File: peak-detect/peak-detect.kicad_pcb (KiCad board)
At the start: 4 copper layers, 33 x 59.7 mm, 70 parts, among them J1 Conn_02x05_Odd_Even, J2 CONN_01X03, J3 CONN_01X03, J4 CONN_01X03, J5 CONN_01X03, Q1 BC847, Q2 BC847, U1 OPA2134, U2 OPA2134, U3 OPA2134

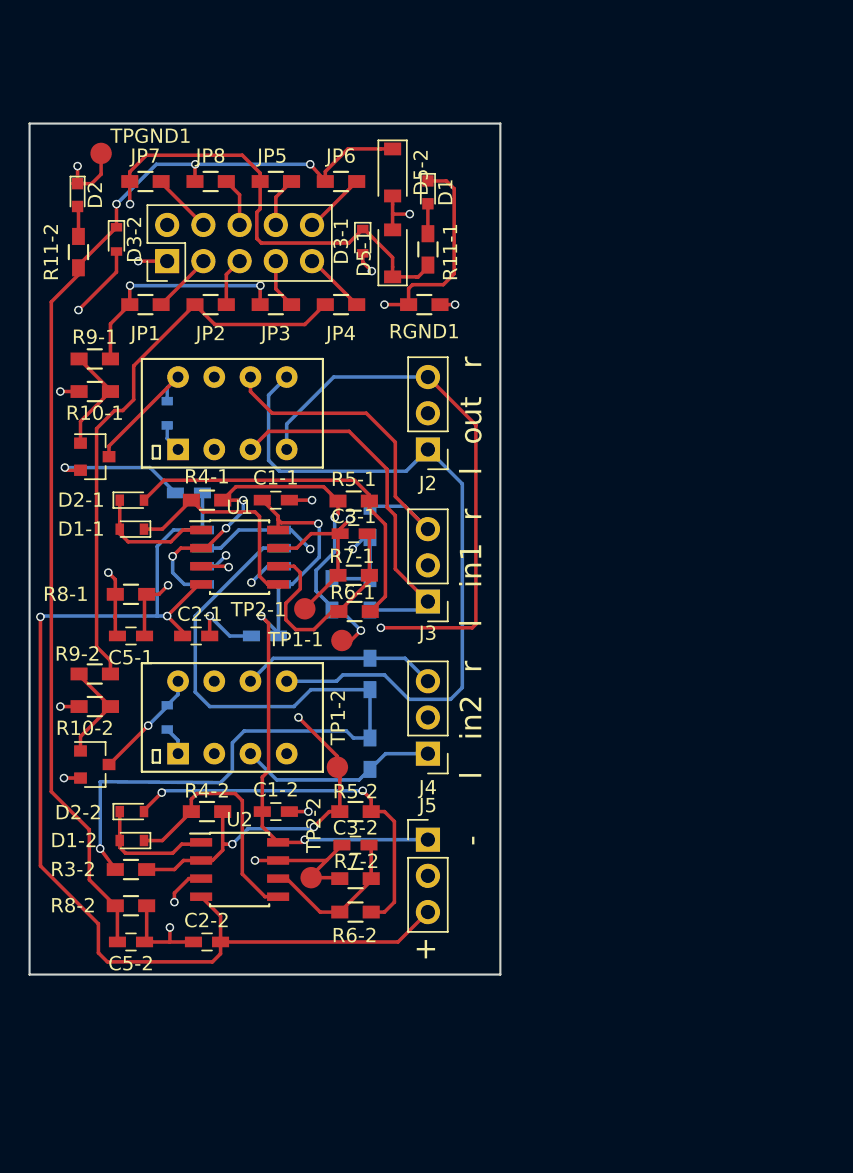
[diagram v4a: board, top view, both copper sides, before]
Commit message: peak-detect: add mixers humidity-sensor: fix bugs, smaller PCB
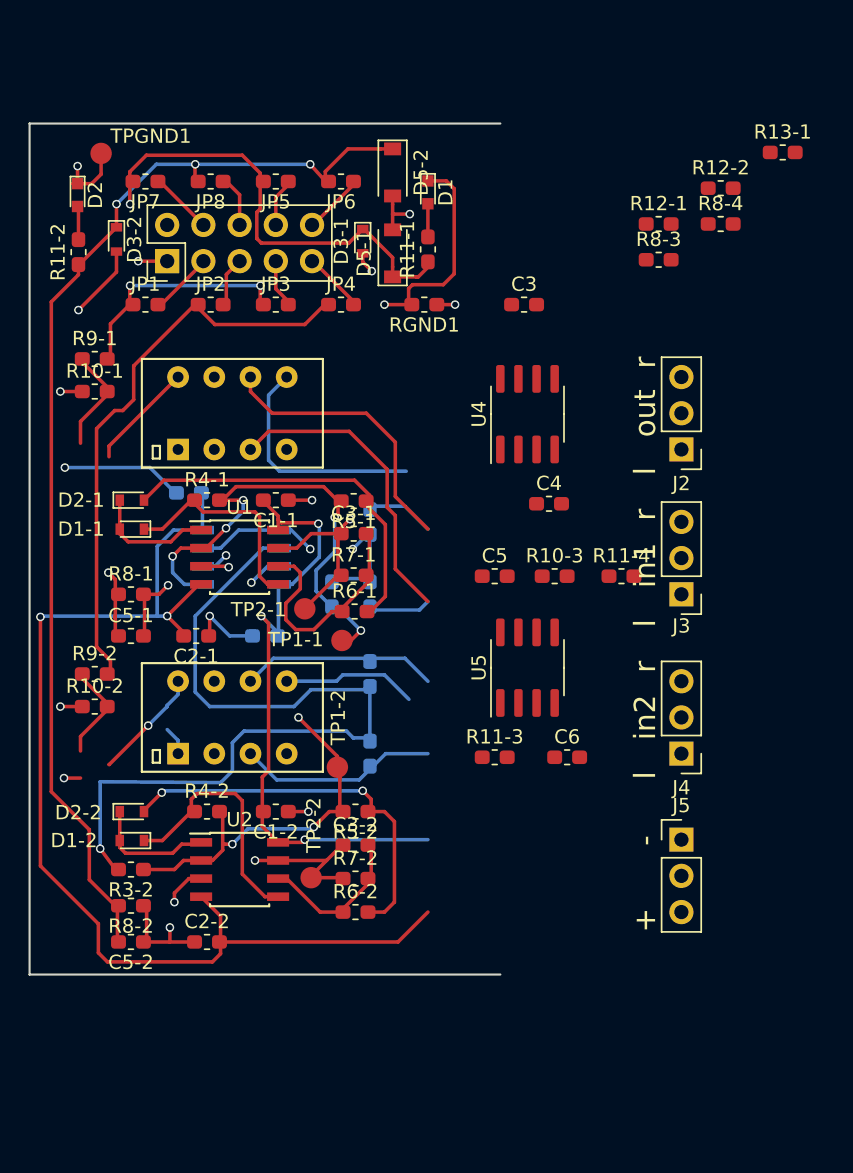
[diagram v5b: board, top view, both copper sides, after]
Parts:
- removed D4-1, D4-2: D, Diodes_SMD:D_0603
- removed Q1, Q2: BC847, TO_SOT_Packages_SMD:SOT-23
- added C3: 100nF, Capacitor_SMD:C_0603_1608Metric_Pad1.05x0.95mm_HandSolder, F.Cu at (192.2, 61.0)
- added C4: 100nF, Capacitor_SMD:C_0603_1608Metric_Pad1.05x0.95mm_HandSolder, F.Cu at (193.9, 74.9)
- added C5: 100nF, Capacitor_SMD:C_0603_1608Metric_Pad1.05x0.95mm_HandSolder, F.Cu at (190.1, 80.0)
- added C6: 100nF, Capacitor_SMD:C_0603_1608Metric_Pad1.05x0.95mm_HandSolder, F.Cu at (195.2, 92.7)
- added R10-3: 10k, Resistor_SMD:R_0603_1608Metric_Pad1.05x0.95mm_HandSolder, F.Cu at (194.3, 80.0)
- added R11-3: 10k, Resistor_SMD:R_0603_1608Metric_Pad1.05x0.95mm_HandSolder, F.Cu at (190.1, 92.7)
- added R11-4: 10k, Resistor_SMD:R_0603_1608Metric_Pad1.05x0.95mm_HandSolder, F.Cu at (199.0, 80.0)
- added R12-1: 10k, Resistor_SMD:R_0603_1608Metric_Pad1.05x0.95mm_HandSolder, F.Cu at (201.6, 55.3)
- added R12-2: 10k, Resistor_SMD:R_0603_1608Metric_Pad1.05x0.95mm_HandSolder, F.Cu at (206.0, 52.8)
- added R13-1: 10k, Resistor_SMD:R_0603_1608Metric_Pad1.05x0.95mm_HandSolder, F.Cu at (210.3, 50.3)
- added R8-3: 10k, Resistor_SMD:R_0603_1608Metric_Pad1.05x0.95mm_HandSolder, F.Cu at (201.6, 57.8)
- added R8-4: 10k, Resistor_SMD:R_0603_1608Metric_Pad1.05x0.95mm_HandSolder, F.Cu at (206.0, 55.3)
- added U4: OPA2134, Package_SO:SOIC-8_3.9x4.9mm_P1.27mm, F.Cu at (192.4, 68.6)
- added U5: OPA2134, Package_SO:SOIC-8_3.9x4.9mm_P1.27mm, F.Cu at (192.4, 86.4)
- C1, C1-1, C1-2, C2, C2-1, C2-2, C3-1, C3-2, C5-1, C5-2: footprint Capacitors_SMD:C_0603_HandSoldering -> Capacitor_SMD:C_0603_1608Metric_Pad1.05x0.95mm_HandSolder
- JP1, JP2, JP3, JP4, JP5, JP6, JP7, JP8, R1-1, R1-2, R11-1, R11-2, R2-1, R2-2, R3-1, R3-2, R4-1, R4-2, R5-1, R5-2, R6-1, R6-2, R7-1, R7-2, R8-1, R8-2, RGND1: footprint Resistors_SMD:R_0603_HandSoldering -> Resistor_SMD:R_0603_1608Metric_Pad1.05x0.95mm_HandSolder
- R10-1, R10-2, R9-1, R9-2: value 1k -> 10k; footprint Resistors_SMD:R_0603_HandSoldering -> Resistor_SMD:R_0603_1608Metric_Pad1.05x0.95mm_HandSolder
- moved J3 17.8 mm to (203.2, 81.3)
- moved J2 17.8 mm to (203.2, 71.1)
- moved J4 17.8 mm to (203.2, 92.5)
- moved J5 17.8 mm to (203.2, 98.5)
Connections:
- R10-1 pad 1: GNDD -> Out-Right-1
- R10-1 pad 2: Net-(Q1-Pad1) -> Net-(R10-1-Pad2)
- R10-2 pad 1: GNDD -> Out-Left-1
- R10-2 pad 2: Net-(Q2-Pad1) -> Net-(R10-2-Pad2)
- R9-1 pad 1: Net-(Q1-Pad1) -> Net-(R10-2-Pad2)
- R9-1 pad 2: Relay-1 -> Out-Left-1
- R9-2 pad 1: Net-(Q2-Pad1) -> Net-(R10-1-Pad2)
- R9-2 pad 2: Relay-2 -> Out-Right-1
- RL1 pad 3: In-Left-1 -> In-Left-2
- RL1 pad 6: In-Right-1 -> In-Right-2
- RL1 pad 8: Net-(D4-1-Pad2) -> Relay-2
- RL2 pad 3: In-Left-2 -> In-Left-1
- RL2 pad 6: In-Right-2 -> In-Right-1
- RL2 pad 8: Net-(D4-2-Pad2) -> Relay-1
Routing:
- net Out-Left: track 52.2 -> 0.00 mm, vias 1 -> 0
- net Out-Right: track 49.7 -> 25.8 mm
- net In-Left-1: track 26.0 -> 4.31 mm
- net In-Left-2: track 14.0 -> 35.6 mm
- net In-Right-2: track 13.8 -> 33.5 mm
- net In-Right-1: track 24.4 -> 4.73 mm
- net Net-(D4-1-Pad2): track 9.60 -> 0.00 mm
- net Net-(D4-2-Pad2): track 7.86 -> 0.00 mm, vias 1 -> 0
- net Relay-1: track 16.2 -> 24.1 mm, vias 2 -> 3
- net Relay-2: track 39.8 -> 47.4 mm
- net GNDD: track 58.2 -> 54.4 mm, vias 13 -> 11
- net +5V: track 49.8 -> 47.8 mm
- net Out-Right-1: track 0.00 -> 1.31 mm, vias 0 -> 1
- net Out-Left-1: track 0.00 -> 1.31 mm, vias 0 -> 1

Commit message: Give peak-detect a mute option
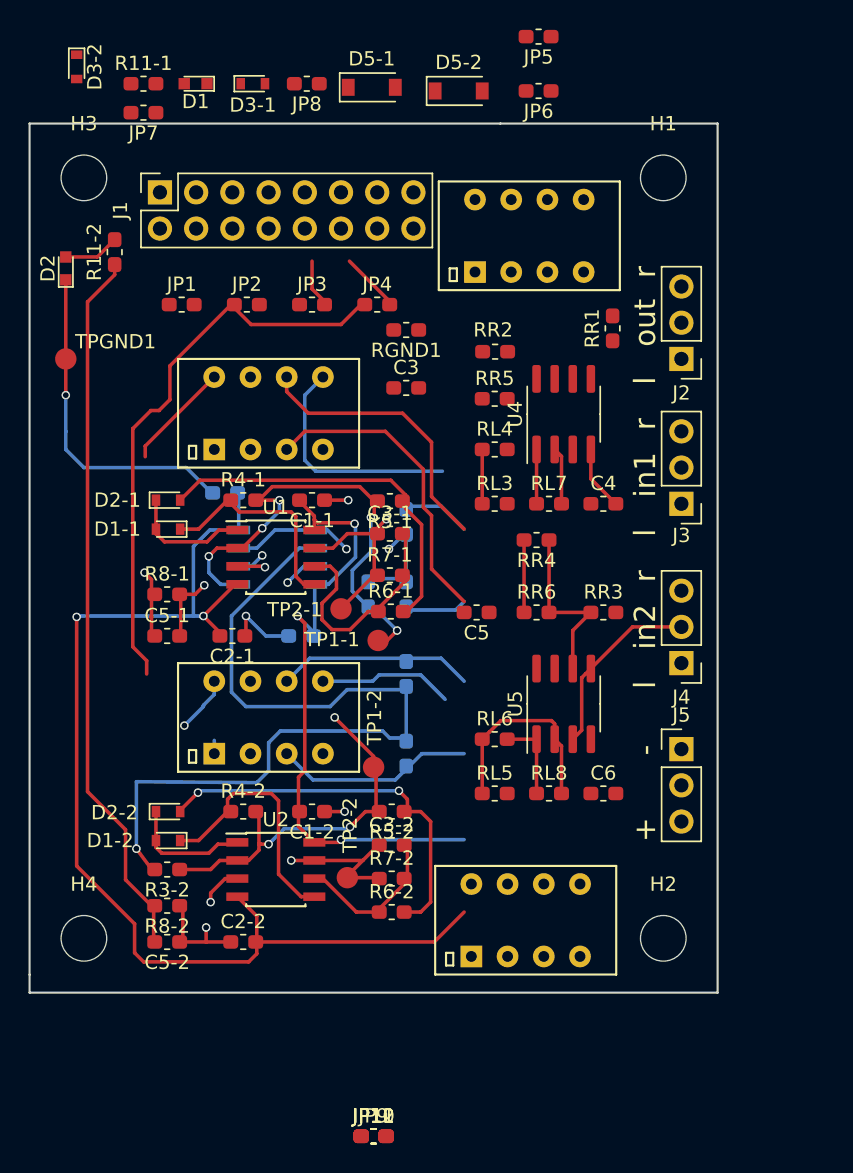
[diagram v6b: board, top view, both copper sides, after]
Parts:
- removed R10-1, R12-1: 10k, Resistor_SMD:R_0603_1608Metric_Pad1.05x0.95mm_HandSolder
- added H1: MountingHole, MountingHole:MountingHole_3.2mm_M3_DIN965, F.Cu at (201.9, 52.1)
- added H2: MountingHole, MountingHole:MountingHole_3.2mm_M3_DIN965, F.Cu at (201.9, 105.4)
- added H3: MountingHole, MountingHole:MountingHole_3.2mm_M3_DIN965, F.Cu at (161.3, 52.1)
- added H4: MountingHole, MountingHole:MountingHole_3.2mm_M3_DIN965, F.Cu at (161.3, 105.4)
- added JP10: Relay-6, Resistor_SMD:R_0603_1608Metric_Pad1.05x0.95mm_HandSolder, F.Cu at (181.6, 119.3)
- added JP11, JP12: Relay-7, Resistor_SMD:R_0603_1608Metric_Pad1.05x0.95mm_HandSolder, F.Cu at (181.6, 119.3)
- added JP9: Relay-5, Resistor_SMD:R_0603_1608Metric_Pad1.05x0.95mm_HandSolder, F.Cu at (181.6, 119.3)
- added RL10: Omron_G6K, lci-kicad:Omron-G6K, F.Cu at (192.3, 104.1)
- added RL6: 10k, Resistor_SMD:R_0603_1608Metric_Pad1.05x0.95mm_HandSolder, F.Cu at (190.1, 91.4)
- added RL9: Omron_G6K, lci-kicad:Omron-G6K, F.Cu at (192.5, 56.1)
- added RR5: 10k, Resistor_SMD:R_0603_1608Metric_Pad1.05x0.95mm_HandSolder, F.Cu at (190.1, 67.6)
- J1: value Conn_02x05_Odd_Even -> Conn_02x08_Odd_Even; footprint Pin_Headers:Pin_Header_Straight_2x05_Pitch2.54mm -> Connector_PinSocket_2.54mm:PinSocket_2x08_P2.54mm_Vertical
- moved RL8 47.9 mm to (193.9, 95.2)
- moved RR2 36.0 mm to (190.1, 64.3), turned to 180 degrees
- moved RL7 34.9 mm to (193.9, 74.9)
- moved RL4 28.8 mm to (190.1, 71.1)
- moved RR4 27.9 mm to (193.0, 77.5), turned to 180 degrees
- moved R11-1 23.1 mm to (165.5, 45.5), turned to 0 degrees
- moved JP5 21.0 mm to (193.2, 42.2)
- moved RL3 20.6 mm to (190.1, 74.9)
- moved D1 18.0 mm to (169.1, 45.5), turned to 180 degrees
- moved JP6 15.2 mm to (193.2, 46.0)
- moved TPGND1 14.6 mm to (160.0, 64.8)
- moved D3-1 13.5 mm to (173.1, 45.5), turned to 0 degrees
- moved D3-2 12.4 mm to (160.8, 44.3)
- moved D5-1 11.7 mm to (181.5, 45.7), turned to 0 degrees
- moved RR1 10.5 mm to (198.4, 62.6), turned to 90 degrees
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- renumbered R1-2 to RL1-1, R1-1 to RL1-2, R8-3 to RL3, R9-1 to RL4, R11-3 to RL5, R10-2 to RL7, R13-1 to RL8, R8-4 to RR1, R2-1 to RR1-1, R9-2 to RR2, R2-2 to RR2-1, R11-4 to RR3, R12-2 to RR4, R10-3 to RR6
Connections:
- net Out-Left-2 renamed Out-Left-Mixed-2
- RL1 pad 3: In-Left-2 -> Out-Left
- RL1 pad 4: Out-Left -> In-Left-2
- RL1 pad 5: Out-Right -> In-Right-2
- RL1 pad 6: In-Right-2 -> Out-Right
- RL2 pad 3: In-Left-1 -> Out-Left
- RL2 pad 4: Out-Left -> In-Left-1
- RL2 pad 5: Out-Right -> In-Right-1
- RL2 pad 6: In-Right-1 -> Out-Right
- RL7 pad 1: Out-Left-1 -> Out-Left-Mixed-1
- RR1 pad 1: Net-(R8-4-Pad1) -> Net-(RR1-Pad1)
- RR2 pad 1: Net-(R10-1-Pad2) -> Net-(RR1-Pad1)
- RR6 pad 1: Out-Right-2 -> Out-Right-Mixed-2
- U4 pad 1: Out-Left-1 -> Out-Left-Mixed-1
- U4 pad 6: Net-(R8-4-Pad1) -> Net-(RR1-Pad1)
- U4 pad 7: Out-Right-1 -> Out-Right-Mixed-1
- U5 pad 7: Out-Right-2 -> Out-Right-Mixed-2
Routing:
- net Out-Peak-1: track 68.2 -> 4.75 mm, vias 2 -> 1
- net Out-Peak-2: track 79.2 -> 50.2 mm, vias 3 -> 0
- net In-Left-2: track 35.6 -> 14.0 mm
- net Out-Left: track 0.00 -> 21.7 mm
- net Relay-1: track 24.1 -> 3.98 mm, vias 3 -> 1
- net +5V: track 47.8 -> 31.2 mm
- net Net-(RL5-Pad1): track 0.00 -> 14.6 mm
- net Net-(RR3-Pad1): track 0.00 -> 12.5 mm
- net GND: track 43.5 -> 55.5 mm, vias 4 -> 3
- net GNDD: track 54.4 -> 43.1 mm, vias 11 -> 6
- net In-Right-1: track 4.73 -> 14.2 mm
- net Net-(RL3-Pad1): track 0.00 -> 7.82 mm
- net Net-(Q1-Pad1): track 7.69 -> 0.00 mm
- net Net-(Q2-Pad1): track 7.18 -> 0.00 mm
- net Out-Right: track 25.8 -> 19.7 mm
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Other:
- board size 33 x 59.7 mm -> 48.3 x 61 mm

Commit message: WIP
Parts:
- moved JP9 67.9 mm to (179.3, 51.4), turned to 270 degrees
- moved JP10 67.9 mm to (181.9, 51.4), turned to 270 degrees
- moved JP11 58.3 mm to (181.9, 61.0), turned to 90 degrees
- moved JP12 58.1 mm to (179.6, 61.2), turned to 90 degrees
- moved D5-2 32.2 mm to (163.1, 66.9), turned to 270 degrees
- moved JP5 26.9 mm to (174.2, 61.3), turned to 270 degrees
- moved JP6 22.5 mm to (176.8, 61.3), turned to 270 degrees
- moved JP8 16.7 mm to (171.7, 61.3), turned to 270 degrees
- moved JP7 14.1 mm to (169.2, 61.1), turned to 270 degrees
- moved JP4 10.8 mm to (176.8, 51.4), turned to 270 degrees
- moved JP3 9.99 mm to (174.2, 51.4), turned to 270 degrees
- moved JP1 9.59 mm to (169.2, 51.4), turned to 270 degrees
- moved JP2 9.58 mm to (171.8, 51.4), turned to 270 degrees
- moved J1 2.03 mm to (166.6, 55.1)
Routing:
- net Relay-2: track 47.4 -> 7.59 mm
- net Net-(J1-Pad9): track 4.31 -> 0.00 mm
- net Net-(J1-Pad7): track 3.50 -> 0.00 mm

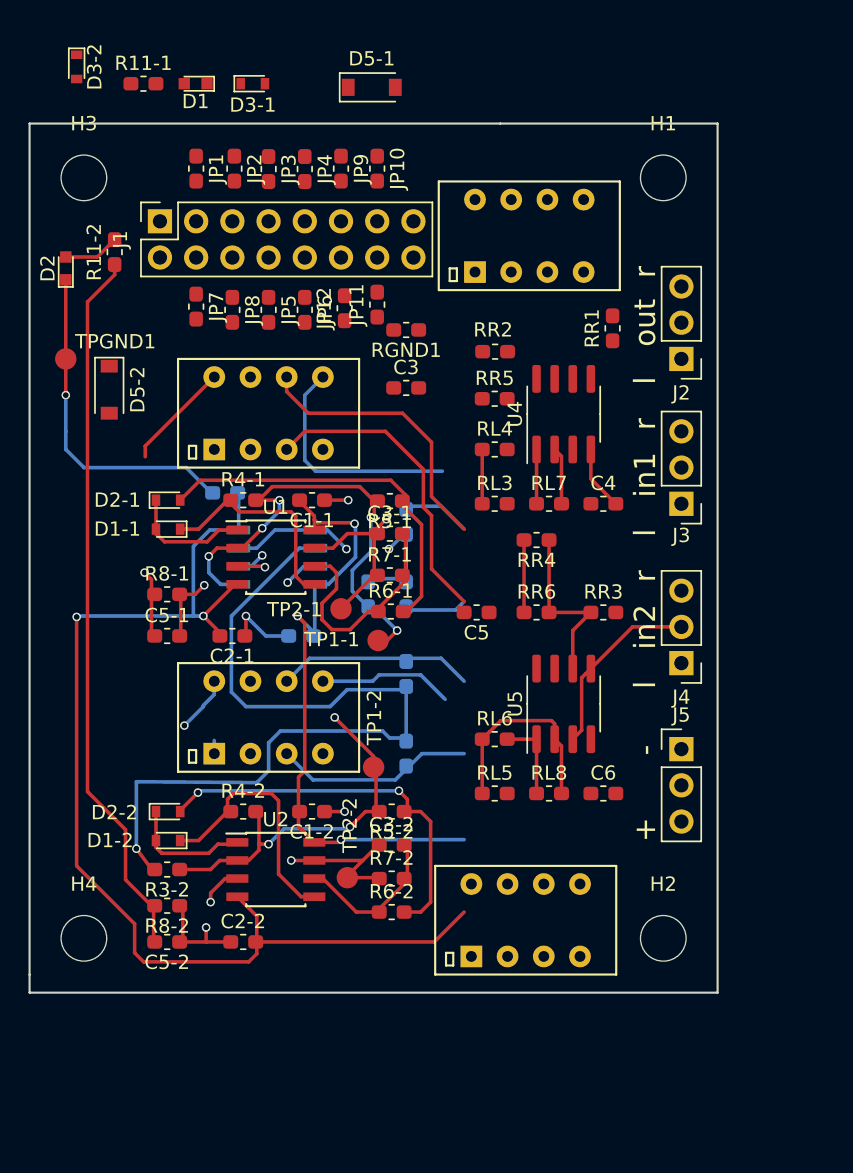
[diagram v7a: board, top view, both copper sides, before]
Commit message: Route mute, mostly automatic changes for peak-detect
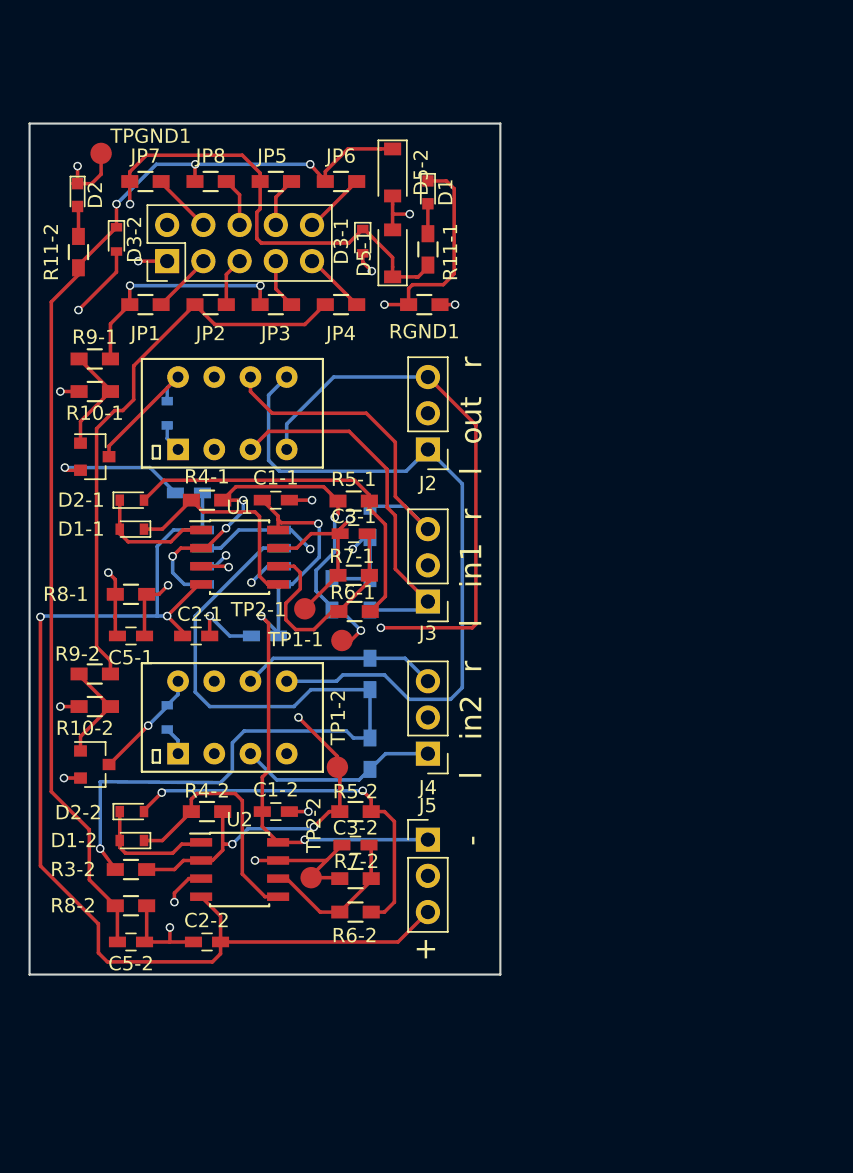
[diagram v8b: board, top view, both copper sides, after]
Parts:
- removed C3, C4, C5, C6: 100nF, Capacitor_SMD:C_0603_1608Metric_Pad1.05x0.95mm_HandSolder
- removed H1, H2, H3, H4: MountingHole, MountingHole:MountingHole_3.2mm_M3_DIN965
- removed JP10: Relay-6, Resistor_SMD:R_0603_1608Metric_Pad1.05x0.95mm_HandSolder
- removed JP11, JP12: Relay-7, Resistor_SMD:R_0603_1608Metric_Pad1.05x0.95mm_HandSolder
- removed JP9: Relay-5, Resistor_SMD:R_0603_1608Metric_Pad1.05x0.95mm_HandSolder
- removed RL1-1, RL1-2, RL3, RL4, RL5, RL6, RL7, RL8, RR1, RR1-1, RR2, RR2-1, RR3, RR4, RR5, RR6: 10k, Resistor_SMD:R_0603_1608Metric_Pad1.05x0.95mm_HandSolder
- removed RL10, RL9: Omron_G6K, lci-kicad:Omron-G6K
- removed U4, U5: OPA2134, Package_SO:SOIC-8_3.9x4.9mm_P1.27mm
- added D4-1: D, Diodes_SMD:D_0603, B.Cu at (167.1, 68.6)
- added D4-2: D, Diodes_SMD:D_0603, B.Cu at (167.1, 89.9)
- added Q1: BC847, TO_SOT_Packages_SMD:SOT-23, F.Cu at (162.1, 71.6)
- added Q2: BC847, TO_SOT_Packages_SMD:SOT-23, F.Cu at (162.1, 93.2)
- added R1-1: 10k, Resistors_SMD:R_0603_HandSoldering, B.Cu at (181.4, 81.3)
- added R1-2: 10k, Resistors_SMD:R_0603_HandSoldering, B.Cu at (181.4, 92.5)
- added R10-1: 1k, Resistors_SMD:R_0603_HandSoldering, F.Cu at (162.1, 67.1)
- added R10-2: 1k, Resistors_SMD:R_0603_HandSoldering, F.Cu at (162.1, 89.2)
- added R2-1: 10k, Resistors_SMD:R_0603_HandSoldering, B.Cu at (181.4, 76.2)
- added R2-2: 10k, Resistors_SMD:R_0603_HandSoldering, B.Cu at (181.4, 86.9)
- added R9-1: 1k, Resistors_SMD:R_0603_HandSoldering, F.Cu at (162.1, 64.8)
- added R9-2: 1k, Resistors_SMD:R_0603_HandSoldering, F.Cu at (162.1, 86.9)
- C1, C1-1, C1-2, C2, C2-1, C2-2, C3-1, C3-2, C5-1, C5-2: footprint Capacitor_SMD:C_0603_1608Metric_Pad1.05x0.95mm_HandSolder -> Capacitors_SMD:C_0603_HandSoldering
- J1: value Conn_02x08_Odd_Even -> Conn_02x05_Odd_Even; footprint Connector_PinSocket_2.54mm:PinSocket_2x08_P2.54mm_Vertical -> Pin_Headers:Pin_Header_Straight_2x05_Pitch2.54mm
- JP1, JP2, JP3, JP4, JP5, JP6, JP7, JP8, R11-1, R11-2, R3-1, R3-2, R4-1, R4-2, R5-1, R5-2, R6-1, R6-2, R7-1, R7-2, R8-1, R8-2, RGND1: footprint Resistor_SMD:R_0603_1608Metric_Pad1.05x0.95mm_HandSolder -> Resistors_SMD:R_0603_HandSoldering
- moved D5-2 25.0 mm to (182.9, 51.7)
- moved R11-1 23.1 mm to (185.4, 57.1), turned to 90 degrees
- moved J3 19.1 mm to (185.4, 81.8)
- moved J2 18.9 mm to (185.4, 71.1)
- moved J4 18.9 mm to (185.4, 92.5)
- moved J5 18.9 mm to (185.4, 98.5)
- moved D1 18.0 mm to (185.4, 53.1), turned to 270 degrees
- moved TPGND1 14.6 mm to (162.5, 50.4)
- moved D3-1 13.5 mm to (180.8, 56.5), turned to 270 degrees
- moved D3-2 12.4 mm to (163.6, 56.4)
- moved D5-1 11.7 mm to (182.9, 57.4), turned to 90 degrees
- moved JP1 10.2 mm to (165.6, 61.0), turned to 0 degrees
- moved JP4 9.84 mm to (179.3, 61.0), turned to 0 degrees
- moved JP2 9.68 mm to (170.2, 61.0), turned to 0 degrees
- moved JP3 9.52 mm to (174.8, 61.0), turned to 0 degrees
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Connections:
- RL1 pad 3: Out-Left -> In-Left-1
- RL1 pad 4: In-Left-2 -> Out-Left
- RL1 pad 5: In-Right-2 -> Out-Right
- RL1 pad 6: Out-Right -> In-Right-1
- RL1 pad 8: Relay-2 -> Net-(D4-1-Pad2)
- RL2 pad 3: Out-Left -> In-Left-2
- RL2 pad 4: In-Left-1 -> Out-Left
- RL2 pad 5: In-Right-1 -> Out-Right
- RL2 pad 6: Out-Right -> In-Right-2
- RL2 pad 8: Relay-1 -> Net-(D4-2-Pad2)
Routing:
- net Out-Peak-1: track 4.75 -> 68.2 mm, vias 1 -> 2
- net Relay-2: track 7.59 -> 39.8 mm
- net Out-Left: track 21.7 -> 52.2 mm, vias 0 -> 1
- net Out-Right: track 19.7 -> 49.7 mm
- net Out-Peak-2: track 50.2 -> 79.2 mm, vias 0 -> 3
- net In-Left-1: track 4.31 -> 26.0 mm
- net +5V: track 31.2 -> 49.8 mm
- net In-Right-2: track 30.1 -> 13.8 mm
- net GNDD: track 43.1 -> 58.2 mm, vias 6 -> 13
- net Net-(RL5-Pad1): track 14.6 -> 0.00 mm
- net Net-(RR3-Pad1): track 12.5 -> 0.00 mm
- net Relay-1: track 3.98 -> 16.2 mm, vias 1 -> 2
- net GND: track 55.5 -> 43.5 mm, vias 3 -> 4
- net In-Right-1: track 14.2 -> 24.4 mm
- net Net-(D4-1-Pad2): track 0.00 -> 9.60 mm
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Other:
- board size 48.3 x 61 mm -> 33 x 59.7 mm
